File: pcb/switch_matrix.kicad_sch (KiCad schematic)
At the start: 94 parts, among them J4 Conn_01x05, J5 Conn_01x05, J6 Conn_01x05, J7 Conn_01x05

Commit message: added some more routing
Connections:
- net COL0 is gone; now on net GP4: D1.1 (K), D13.1 (K), D7.1 (K)
- net COL10 is gone; now on net GP12: J6.4 (Pin_4)
- net COL11 is gone; now on net GP11: J6.5 (Pin_5)
- net COL3 is gone; now on net GP7: D10.1 (K), D16.1 (K), D20.1 (K), D4.1 (K)
- net COL4 is gone; now on net GP8: D11.1 (K), D17.1 (K), D21.1 (K), D5.1 (K)
- net COL5 is gone; now on net GP9: D12.1 (K), D18.1 (K), D22.1 (K), D6.1 (K)
- net COL6 is gone; now on net GP0: J4.5 (Pin_5)
- net COL7 is gone; now on net GP15: J6.1 (Pin_1)
- net COL8 is gone; now on net GP14: J6.2 (Pin_2)
- net COL9 is gone; now on net GP13: J6.3 (Pin_3)
- net GP0: now also MX1.1, MX2.1, MX3.1, MX4.1, MX5.1, MX6.1; no longer J4.2 (Pin_2), J5.2 (Pin_2), MX10.1, MX11.1, MX12.1, MX7.1, MX8.1, MX9.1
- net GP1: now also J4.4 (Pin_4), MX10.1, MX11.1, MX12.1, MX7.1, MX8.1, MX9.1; no longer J4.3 (Pin_3), J5.3 (Pin_3), MX13.1, MX14.1, MX15.1, MX16.1, MX17.1, MX18.1
- net GP10: now also J4.1 (Pin_1)
- net GP2: now also J4.3 (Pin_3), MX13.1, MX14.1, MX15.1, MX16.1, MX17.1, MX18.1; no longer D14.1 (K), D2.1 (K), D8.1 (K)
- net GP3: now also J4.2 (Pin_2), MX19.1, MX20.1, MX21.1, MX22.1, MX45.1; no longer D15.1 (K), D19.1 (K), D3.1 (K), D9.1 (K)
- net GP5: now also D14.1 (K), D2.1 (K), D8.1 (K)
- net GP6: now also D15.1 (K), D19.1 (K), D3.1 (K), D9.1 (K)
- net ROW0r: now also J5.1 (Pin_1)
- net ROW1r: now also J5.2 (Pin_2)
- net ROW2r: now also J5.3 (Pin_3)
- net ROW3r: now also J5.4 (Pin_4)
- removed net ROW0: J4.1 (Pin_1), J5.1 (Pin_1), MX1.1, MX2.1, MX3.1, MX4.1, MX5.1, MX6.1
- removed net ROW3: J4.4 (Pin_4), J5.4 (Pin_4), MX19.1, MX20.1, MX21.1, MX22.1, MX45.1
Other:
- moved on the sheet: J4, J5, J6, J7
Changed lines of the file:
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@@
 		)
 	)
-	(label "ROW1"
-		(at 139.7 27.94 180)
+	(label "COL11"
+		(at 16.51 59.69 180)
 		(effects
 			(font
@@
 	)
 	(label "COL6r"
-		(at 165.1 35.56 180)
+		(at 158.75 38.1 180)
 		(effects
 			(font
@@
 		)
 	)
-	(label "ROW0"
-		(at 139.7 25.4 180)
+	(label "COL2"
+		(at 16.51 36.83 180)
+		(effects
+			(font
+				(size 1.27 1.27)
+			)
+			(justify right bottom)
+		)
+	)
+	(label "ROW3"
+		(at 133.35 30.48 180)
 		(effects
 			(font
@@
 		)
 	)
+	(label "COL5"
+		(at 16.51 44.45 180)
+		(effects
+			(font
+				(size 1.27 1.27)
+			)
+			(justify right bottom)
+		)
+	)
 	(label "COL8"
-		(at 139.7 41.91 180)
+		(at 133.35 49.53 180)
 		(effects
 			(font
@@
 	)
 	(label "COL7"
-		(at 139.7 39.37 180)
+		(at 133.35 52.07 180)
 		(effects
 			(font
@@
 		)
 	)
-	(label "ROW2"
-		(at 165.1 30.48 180)
+	(label "ROW2r"
+		(at 158.75 33.02 180)
 		(effects
 			(font
@@
 	)
 	(label "COL6"
-		(at 139.7 35.56 180)
+		(at 133.35 27.94 180)
 		(effects
 			(font
@@
 	)
 	(label "COL8r"
-		(at 165.1 41.91 180)
+		(at 158.75 44.45 180)
 		(effects
 			(font
@@
 		)
 	)
-	(label "COL2"
-		(at 16.51 29.21 180)
+	(label "ROW0"
+		(at 16.51 21.59 180)
+		(effects
+			(font
+				(size 1.27 1.27)
+			)
+			(justify right bottom)
+		)
+	)
+	(label "COL6"
+		(at 16.51 46.99 180)
+		(effects
+			(font
+				(size 1.27 1.27)
+			)
+			(justify right bottom)
+		)
+	)
+	(label "COL10"
+		(at 16.51 57.15 180)
 		(effects
 			(font
@@
 	)
 	(label "COL10r"
-		(at 165.1 46.99 180)
+		(at 158.75 49.53 180)
 		(effects
 			(font
@@
 	)
 	(label "ROW1"
-		(at 16.51 21.59 180)
+		(at 16.51 24.13 180)
 		(effects
 			(font
@@
 	)
 	(label "COL11r"
-		(at 165.1 49.53 180)
+		(at 158.75 52.07 180)
 		(effects
 			(font
@@
 		)
 	)
-	(label "ROW1"
-		(at 165.1 27.94 180)
+	(label "COL7"
+		(at 16.51 49.53 180)
+		(effects
+			(font
+				(size 1.27 1.27)
+			)
+			(justify right bottom)
+		)
+	)
+	(label "ROW1r"
+		(at 158.75 30.48 180)
 		(effects
 			(font
@@
 	)
 	(label "COL9r"
-		(at 165.1 44.45 180)
+		(at 158.75 46.99 180)
 		(effects
 			(font
@@
 		)
 	)
-	(label "ROW3"
-		(at 139.7 33.02 180)
+	(label "COL1"
+		(at 16.51 34.29 180)
+		(effects
+			(font
+				(size 1.27 1.27)
+			)
+			(justify right bottom)
+		)
+	)
+	(label "COL3"
+		(at 16.51 39.37 180)
 		(effects
 			(font
@@
 		)
 	)
+	(label "ROW3"
+		(at 16.51 29.21 180)
+		(effects
+			(font
+				(size 1.27 1.27)
+			)
+			(justify right bottom)
+		)
+	)
 	(label "COL9"
-		(at 139.7 44.45 180)
+		(at 133.35 46.99 180)
 		(effects
 			(font
@@
 	)
 	(label "COL7r"
-		(at 165.1 39.37 180)
+		(at 158.75 41.91 180)
+		(effects
+			(font
+				(size 1.27 1.27)
+			)
+			(justify right bottom)
+		)
+	)
+	(label "COL8"
+		(at 16.51 52.07 180)
+		(effects
+			(font
+				(size 1.27 1.27)
+			)
+			(justify right bottom)
+		)
+	)
+	(label "COL4"
+		(at 16.51 41.91 180)
+		(effects
+			(font
+				(size 1.27 1.27)
+			)
+			(justify right bottom)
+		)
+	)
+	(label "COL9"
+		(at 16.51 54.61 180)
+		(effects
+			(font
+				(size 1.27 1.27)
+			)
+			(justify right bottom)
+		)
+	)
+	(label "ROW0"
+		(at 133.35 38.1 180)
 		(effects
 			(font
@@
 	)
 	(label "ROW2"
-		(at 16.51 24.13 180)
+		(at 16.51 26.67 180)
 		(effects
 			(font
@@
 	)
 	(label "COL11"
-		(at 139.7 49.53 180)
+		(at 133.35 41.91 180)
 		(effects
 			(font
@@
 		)
 	)
-	(label "ROW3"
-		(at 165.1 33.02 180)
+	(label "ROW3r"
+		(at 158.75 35.56 180)
 		(effects
 			(font
@@
 	)
 	(label "ROW2"
-		(at 139.7 30.48 180)
+		(at 133.35 33.02 180)
 		(effects
 			(font
@@
 	)
 	(label "COL10"
-		(at 139.7 46.99 180)
+		(at 133.35 44.45 180)
+		(effects
+			(font
+				(size 1.27 1.27)
+			)
+			(justify right bottom)
+		)
+	)
+	(label "COL0"
+		(at 16.51 31.75 180)
 		(effects
 			(font
@@
 		)
 	)
-	(label "ROW0"
-		(at 165.1 25.4 180)
+	(label "ROW1"
+		(at 133.35 35.56 180)
 		(effects
 			(font
@@
 		)
 	)
-	(label "COL1"
-		(at 16.51 26.67 180)
+	(label "ROW0r"
+		(at 158.75 27.94 180)
 		(effects
 			(font
@@
 	(symbol
 		(lib_id "Connector_Generic:Conn_01x05")
-		(at 144.78 30.48 0)
+		(at 138.43 33.02 0)
 		(unit 1)
 		(exclude_from_sim no)
@@
 		(fields_autoplaced yes)
 		(property "Reference" "J4"
-			(at 147.32 29.2099 0)
+			(at 140.97 31.7499 0)
 			(effects
 				(font
@@
 		)
 		(property "Value" "Conn_01x05"
-			(at 147.32 31.7499 0)
+			(at 140.97 34.2899 0)
 			(effects
 				(font
@@
 		)
 		(property "Footprint" "Connector_JST:JST_GH_SM05B-GHS-TB_1x05-1MP_P1.25mm_Horizontal"
-			(at 144.78 30.48 0)
+			(at 138.43 33.02 0)
 			(effects
 				(font
@@
 		)
 		(property "Datasheet" "~"
-			(at 144.78 30.48 0)
+			(at 138.43 33.02 0)
 			(effects
 				(font
@@
 		)
 		(property "Description" "Generic connector, single row, 01x05, script generated (kicad-library-utils/schlib/autogen/connector/)"
-			(at 144.78 30.48 0)
+			(at 138.43 33.02 0)
 			(effects
 				(font
@@
 	(symbol
 		(lib_id "Connector_Generic:Conn_01x05")
-		(at 170.18 30.48 0)
+		(at 163.83 33.02 0)
 		(unit 1)
 		(exclude_from_sim no)
@@
 		(fields_autoplaced yes)
 		(property "Reference" "J5"
-			(at 172.72 29.2099 0)
+			(at 166.37 31.7499 0)
 			(effects
 				(font
@@
 		)
 		(property "Value" "Conn_01x05"
-			(at 172.72 31.7499 0)
+			(at 166.37 34.2899 0)
 			(effects
 				(font
@@
 		)
 		(property "Footprint" "Connector_JST:JST_GH_SM05B-GHS-TB_1x05-1MP_P1.25mm_Horizontal"
-			(at 170.18 30.48 0)
+			(at 163.83 33.02 0)
 			(effects
 				(font
@@
 		)
 		(property "Datasheet" "~"
-			(at 170.18 30.48 0)
+			(at 163.83 33.02 0)
 			(effects
 				(font
@@
 		)
 		(property "Description" "Generic connector, single row, 01x05, script generated (kicad-library-utils/schlib/autogen/connector/)"
-			(at 170.18 30.48 0)
+			(at 163.83 33.02 0)
 			(effects
 				(font
@@
 	(symbol
 		(lib_id "Connector_Generic:Conn_01x05")
-		(at 170.18 44.45 0)
+		(at 163.83 46.99 0)
 		(unit 1)
 		(exclude_from_sim no)
@@
 		(fields_autoplaced yes)
 		(property "Reference" "J7"
-			(at 172.72 43.1799 0)
+			(at 166.37 45.7199 0)
 			(effects
 				(font
@@
 		)
 		(property "Value" "Conn_01x05"
-			(at 172.72 45.7199 0)
+			(at 166.37 48.2599 0)
 			(effects
 				(font
@@
 		)
 		(property "Footprint" "Connector_JST:JST_GH_SM05B-GHS-TB_1x05-1MP_P1.25mm_Horizontal"
-			(at 170.18 44.45 0)
+			(at 163.83 46.99 0)
 			(effects
 				(font
@@
 		)
 		(property "Datasheet" "~"
-			(at 170.18 44.45 0)
+			(at 163.83 46.99 0)
 			(effects
 				(font
@@
 		)
 		(property "Description" "Generic connector, single row, 01x05, script generated (kicad-library-utils/schlib/autogen/connector/)"
-			(at 170.18 44.45 0)
+			(at 163.83 46.99 0)
 			(effects
 				(font
@@
 	(symbol
 		(lib_id "Connector_Generic:Conn_01x05")
-		(at 144.78 44.45 0)
+		(at 138.43 46.99 0)
 		(unit 1)
 		(exclude_from_sim no)
@@
 		(fields_autoplaced yes)
 		(property "Reference" "J6"
-			(at 147.32 43.1799 0)
+			(at 140.97 45.7199 0)
 			(effects
 				(font
@@
 		)
 		(property "Value" "Conn_01x05"
-			(at 147.32 45.7199 0)
+			(at 140.97 48.2599 0)
 			(effects
 				(font
@@
 		)
 		(property "Footprint" "Connector_JST:JST_GH_SM05B-GHS-TB_1x05-1MP_P1.25mm_Horizontal"
-			(at 144.78 44.45 0)
+			(at 138.43 46.99 0)
 			(effects
 				(font
@@
 		)
 		(property "Datasheet" "~"
-			(at 144.78 44.45 0)
+			(at 138.43 46.99 0)
 			(effects
 				(font
@@
 		)
 		(property "Description" "Generic connector, single row, 01x05, script generated (kicad-library-utils/schlib/autogen/connector/)"
-			(at 144.78 44.45 0)
+			(at 138.43 46.99 0)
 			(effects
 				(font

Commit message: redid routing
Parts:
- removed J4, J5, J6, J7: Conn_01x05, Connector_JST:JST_GH_SM05B-GHS-TB_1x05-1MP_P1.25mm_Horizontal, symbol Connector_Generic:Conn_01x05
- added J2, J3: Conn_01x10, Connector_JST:JST_GH_SM10B-GHS-TB_1x10-1MP_P1.25mm_Horizontal, symbol Connector_Generic:Conn_01x10
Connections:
- net COL10r: now also J3.9 (Pin_9)
- net COL11r: now also J3.10 (Pin_10)
- net COL6r: now also J3.5 (Pin_5)
- net COL7r: now also J3.6 (Pin_6)
- net COL8r: now also J3.7 (Pin_7)
- net COL9r: now also J3.8 (Pin_8)
- net GP0: no longer MX1.1, MX2.1, MX3.1, MX4.1, MX5.1, MX6.1
- net GP1: now also MX1.1, MX2.1, MX3.1, MX4.1, MX5.1, MX6.1, J2.10 (Pin_10); no longer MX10.1, MX11.1, MX12.1, MX7.1, MX8.1, MX9.1
- net GP11: now also J2.6 (Pin_6)
- net GP12: now also J2.5 (Pin_5)
- net GP13: now also J2.4 (Pin_4)
- net GP14: now also J2.3 (Pin_3)
- net GP15: now also J2.2 (Pin_2)
- net GP16: now also J2.1 (Pin_1)
- net GP2: now also MX10.1, MX11.1, MX12.1, MX7.1, MX8.1, MX9.1, J2.9 (Pin_9); no longer MX13.1, MX14.1, MX15.1, MX16.1, MX17.1, MX18.1
- net GP23: now also D15.1 (K), D19.1 (K), D3.1 (K), D9.1 (K)
- net GP24: now also D10.1 (K), D16.1 (K), D20.1 (K), D4.1 (K)
- net GP28: now also D12.1 (K), D18.1 (K), D22.1 (K), D6.1 (K)
- net GP29: now also D11.1 (K), D17.1 (K), D21.1 (K), D5.1 (K)
- net GP3: now also MX13.1, MX14.1, MX15.1, MX16.1, MX17.1, MX18.1, J2.8 (Pin_8); no longer MX19.1, MX20.1, MX21.1, MX22.1, MX45.1
- net GP4: now also MX19.1, MX20.1, MX21.1, MX22.1, MX45.1, J2.7 (Pin_7); no longer D1.1 (K), D13.1 (K), D7.1 (K)
- net GP5: now also D1.1 (K), D13.1 (K), D7.1 (K); no longer D14.1 (K), D2.1 (K), D8.1 (K)
- net GP6: now also D14.1 (K), D2.1 (K), D8.1 (K); no longer D15.1 (K), D19.1 (K), D3.1 (K), D9.1 (K)
- net GP7: no longer D10.1 (K), D16.1 (K), D20.1 (K), D4.1 (K)
- net GP8: no longer D11.1 (K), D17.1 (K), D21.1 (K), D5.1 (K)
- net GP9: no longer D12.1 (K), D18.1 (K), D22.1 (K), D6.1 (K)
- net ROW0r: now also J3.1 (Pin_1)
- net ROW1r: now also J3.2 (Pin_2)
- net ROW2r: now also J3.3 (Pin_3)
- net ROW3r: now also J3.4 (Pin_4)

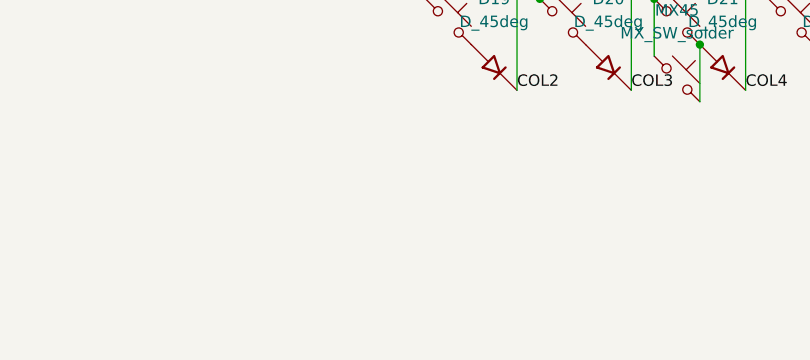
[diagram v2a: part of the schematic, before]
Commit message: added silk, panels and stabs
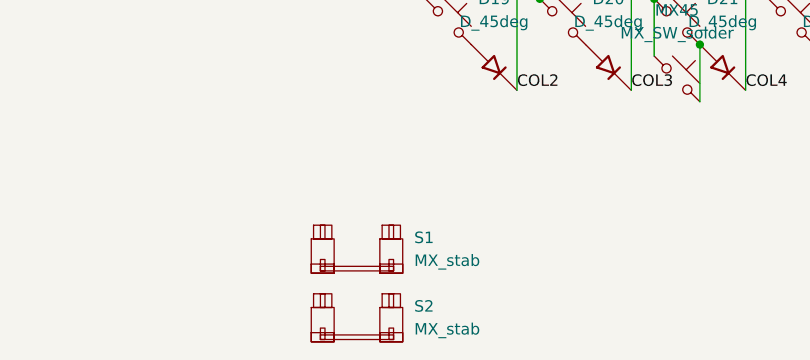
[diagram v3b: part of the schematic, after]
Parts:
- added S1, S2: MX_stab, PCM_marbastlib-mx:STAB_MX_P_2u, symbol PCM_marbastlib-mx:MX_stab
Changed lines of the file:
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@@
 	)
 	(symbol
+		(lib_id "PCM_marbastlib-mx:MX_stab")
+		(at 77.47 165.1 0)
+		(unit 1)
+		(exclude_from_sim no)
+		(in_bom yes)
+		(on_board yes)
+		(dnp no)
+		(fields_autoplaced yes)
+		(property "Reference" "S2"
+			(at 83.82 163.7029 0)
+			(effects
+				(font
+					(size 1.27 1.27)
+				)
+				(justify left)
+			)
+		)
+		(property "Value" "MX_stab"
+			(at 83.82 166.2429 0)
+			(effects
+				(font
+					(size 1.27 1.27)
+				)
+				(justify left)
+			)
+		)
+		(property "Footprint" "PCM_marbastlib-mx:STAB_MX_P_2u"
+			(at 77.47 165.1 0)
+			(effects
+				(font
+					(size 1.27 1.27)
+				)
+				(hide yes)
+			)
+		)
+		(property "Datasheet" ""
+			(at 77.47 165.1 0)
+			(effects
+				(font
+					(size 1.27 1.27)
+				)
+				(hide yes)
+			)
+		)
+		(property "Description" "Cherry MX-style stabilizer"
+			(at 77.47 165.1 0)
+			(effects
+				(font
+					(size 1.27 1.27)
+				)
+				(hide yes)
+			)
+		)
+		(instances
+			(project "pcb"
+				(path "/dea5f69c-d02e-47df-8e1a-a63949fabb21/0cbd56a0-84b2-4041-9681-83c3815281ca"
+					(reference "S2")
+					(unit 1)
+				)
+			)
+		)
+	)
+	(symbol
 		(lib_id "PCM_marbastlib-mx:MX_SW_solder")
 		(at 100.33 78.74 0)
@@
 					(unit 1)
 				)
+			)
+		)
+	)
+	(symbol
+		(lib_id "PCM_marbastlib-mx:MX_stab")
+		(at 77.47 157.48 0)
+		(unit 1)
+		(exclude_from_sim no)
+		(in_bom yes)
+		(on_board yes)
+		(dnp no)
+		(fields_autoplaced yes)
+		(property "Reference" "S1"
+			(at 83.82 156.0829 0)
+			(effects
+				(font
+					(size 1.27 1.27)
+				)
+				(justify left)
+			)
+		)
+		(property "Value" "MX_stab"
+			(at 83.82 158.6229 0)
+			(effects
+				(font
+					(size 1.27 1.27)
+				)
+				(justify left)
+			)
+		)
+		(property "Footprint" "PCM_marbastlib-mx:STAB_MX_P_2u"
+			(at 77.47 157.48 0)
+			(effects
+				(font
+					(size 1.27 1.27)
+				)
+				(hide yes)
+			)
+		)
+		(property "Datasheet" ""
+			(at 77.47 157.48 0)
+			(effects
+				(font
+					(size 1.27 1.27)
+				)
+				(hide yes)
+			)
+		)
+		(property "Description" "Cherry MX-style stabilizer"
+			(at 77.47 157.48 0)
+			(effects
+				(font
+					(size 1.27 1.27)
+				)
+				(hide yes)
+			)
+		)
+		(instances
+			(project ""
+				(path "/dea5f69c-d02e-47df-8e1a-a63949fabb21/0cbd56a0-84b2-4041-9681-83c3815281ca"
+					(reference "S1")
+					(unit 1)
+				)
